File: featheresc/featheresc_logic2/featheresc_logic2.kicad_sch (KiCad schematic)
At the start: 24 parts, among them J1 RC IN 1, J2 RC IN 2, J3 soicbite prog connector, J7 Interconnect 1, J8 Interconnect 2, U1 AMS1117-50, U2 XL1509-ADJE1, U3 ATtiny1614-SS

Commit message: Update layout to be more compact, swap a few parts
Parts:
- J1, J2: footprint Connector_JST:JST_XA_S03B-XASK-1_1x03_P2.50mm_Horizontal -> Connector_JST:JST_XH_S3B-XH-A_1x03_P2.50mm_Horizontal
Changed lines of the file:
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@@
       (effects (font (size 1.27 1.27)) (justify right))
     )
-    (property "Footprint" "Connector_JST:JST_XA_S03B-XASK-1_1x03_P2.50mm_Horizontal" (id 2) (at 193.04 153.035 0)
+    (property "Footprint" "Connector_JST:JST_XH_S3B-XH-A_1x03_P2.50mm_Horizontal" (id 2) (at 193.04 153.035 0)
       (effects (font (size 1.27 1.27)) hide)
     )
@@
       (effects (font (size 1.27 1.27)) (justify right))
     )
-    (property "Footprint" "Connector_JST:JST_XA_S03B-XASK-1_1x03_P2.50mm_Horizontal" (id 2) (at 245.11 153.035 0)
+    (property "Footprint" "Connector_JST:JST_XH_S3B-XH-A_1x03_P2.50mm_Horizontal" (id 2) (at 245.11 153.035 0)
       (effects (font (size 1.27 1.27)) hide)
     )
@@
       (reference "#PWR04") (unit 1) (value "GND") (footprint "")
     )
-    (path "/d7d4c434-72cc-459d-9ec2-c8f3576f629f/52343ac2-4969-42df-af1e-ed7deb794aea"
-      (reference "#PWR05") (unit 1) (value "GND") (footprint "")
-    )
     (path "/96d38acb-e23b-424c-afed-fdd96c395092"
       (reference "#PWR06") (unit 1) (value "GND") (footprint "")
@@
       (reference "#PWR018") (unit 1) (value "GND") (footprint "")
     )
-    (path "/e21eb0e0-0c12-4a19-b0a2-2a3e790fd264/52343ac2-4969-42df-af1e-ed7deb794aea"
-      (reference "#PWR019") (unit 1) (value "GND") (footprint "")
-    )
     (path "/acde64c0-adac-4ba4-8f88-518b3a754432"
       (reference "#PWR020") (unit 1) (value "GND") (footprint "")
@@
       (reference "D8") (unit 1) (value "Red") (footprint "LED_SMD:LED_0805_2012Metric_Pad1.15x1.40mm_HandSolder")
     )
+    (path "/d7d4c434-72cc-459d-9ec2-c8f3576f629f/11cdec55-435f-4b7f-805a-bee9ab2b00ee"
+      (reference "D9") (unit 1) (value "Green") (footprint "LED_SMD:LED_0805_2012Metric_Pad1.15x1.40mm_HandSolder")
+    )
+    (path "/e21eb0e0-0c12-4a19-b0a2-2a3e790fd264/11cdec55-435f-4b7f-805a-bee9ab2b00ee"
+      (reference "D10") (unit 1) (value "Green") (footprint "LED_SMD:LED_0805_2012Metric_Pad1.15x1.40mm_HandSolder")
+    )
     (path "/232bbb65-7869-4831-a033-eb4672019cff"
       (reference "H1") (unit 1) (value "Interconnect M3") (footprint "MountingHole:MountingHole_3.2mm_M3")
@@
     )
     (path "/006e2d2d-ea55-4517-8464-6fa4323dbbb5"
-      (reference "J1") (unit 1) (value "RC IN 1") (footprint "Connector_JST:JST_XA_S03B-XASK-1_1x03_P2.50mm_Horizontal")
+      (reference "J1") (unit 1) (value "RC IN 1") (footprint "Connector_JST:JST_XH_S3B-XH-A_1x03_P2.50mm_Horizontal")
     )
     (path "/e6790c5d-2c5e-4728-8d92-8b5fc4b99492"
-      (reference "J2") (unit 1) (value "RC IN 2") (footprint "Connector_JST:JST_XA_S03B-XASK-1_1x03_P2.50mm_Horizontal")
+      (reference "J2") (unit 1) (value "RC IN 2") (footprint "Connector_JST:JST_XH_S3B-XH-A_1x03_P2.50mm_Horizontal")
     )
     (path "/8881e0dd-f100-4ed2-ac37-7908cdabe46b"

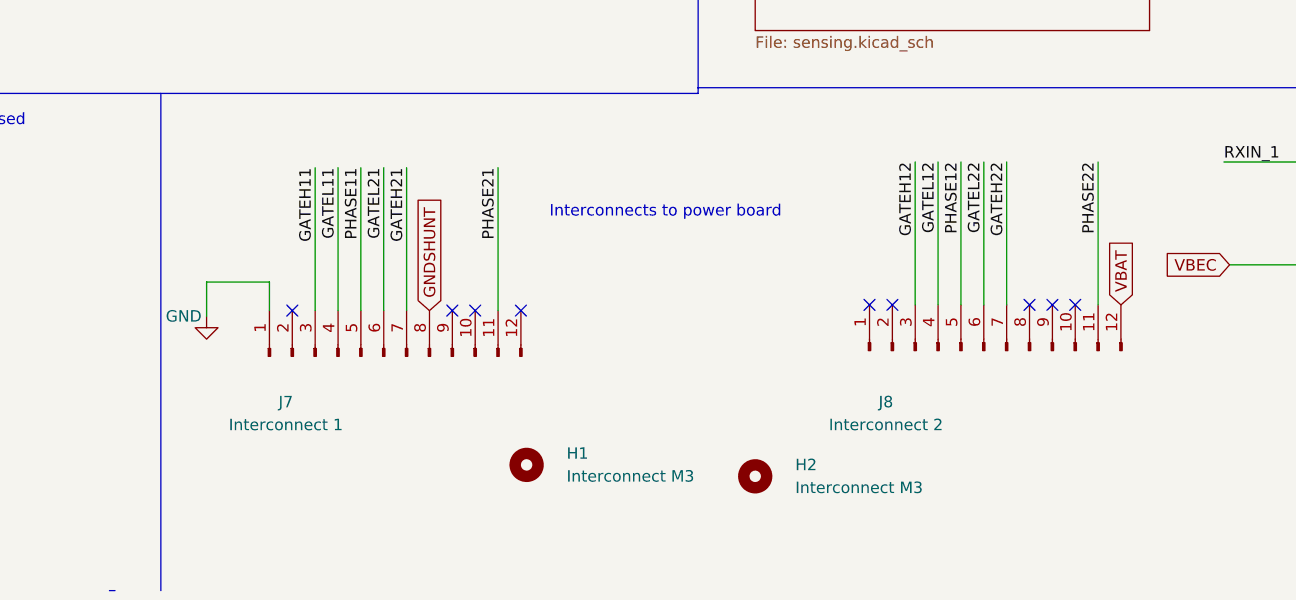
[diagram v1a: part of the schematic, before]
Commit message: improve interconnect pinouts
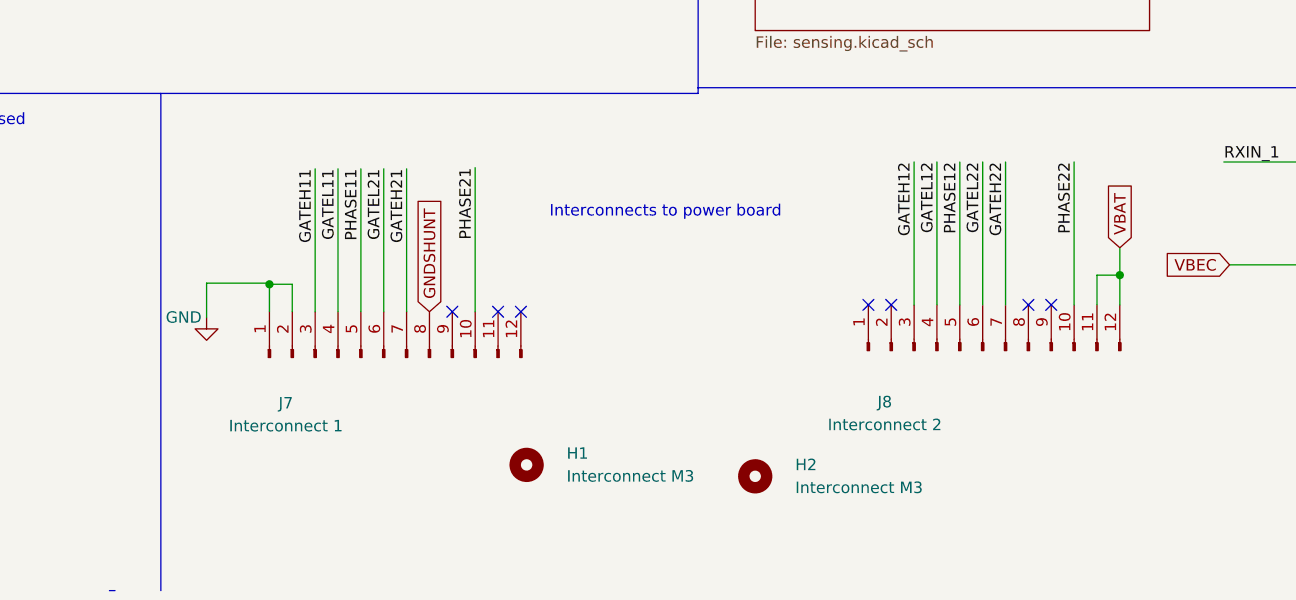
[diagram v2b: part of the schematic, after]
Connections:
- net GND: now also J7.2 (Pin_2)
- net PHASE21: now also J7.10 (Pin_10); no longer J7.11 (Pin_11)
- net PHASE22: now also J8.10 (Pin_10); no longer J8.11 (Pin_11)
- net VBAT: now also J8.11 (Pin_11)
- no-connect marks 14 -> 12

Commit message: Mixing switch
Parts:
- added R5: 33k, Resistor_SMD:R_0603_1608Metric_Pad0.98x0.95mm_HandSolder, symbol Device:R
- added SW1: SW_DIP_x01, Button_Switch_THT:SW_DIP_SPSTx01_Slide_6.7x4.1mm_W7.62mm_P2.54mm_LowProfile, symbol Switch:SW_DIP_x01
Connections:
- net GND: now also R5.2
- net TXDEBUG: now also SW1.1
- new net: R5.1, SW1.2
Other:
- note added: "Mixing on/off switch"
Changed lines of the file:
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@@
+    (stroke (width 0) (type default) (color 0 0 0 0))
+  )
+  (wire (pts (xy 79.248 113.538) (xy 79.248 118.618))
     (stroke (width 0) (type default) (color 0 0 0 0))
   )
@@
     (stroke (width 0) (type default) (color 0 0 0 0))
   )
+  (wire (pts (xy 53.848 113.538) (xy 36.703 113.538))
+    (stroke (width 0) (type default) (color 0 0 0 0))
+  )
   (wire (pts (xy 74.93 43.815) (xy 80.645 43.815))
     (stroke (width 0) (type default) (color 0 0 0 0))
@@
     (stroke (width 0) (type default) (color 0 0 0 0))
   )
+  (wire (pts (xy 76.708 113.538) (xy 79.248 113.538))
+    (stroke (width 0) (type default) (color 0 0 0 0))
+  )
   (wire (pts (xy 128.27 98.425) (xy 128.27 111.125))
     (stroke (width 0) (type default) (color 0 0 0 0))
@@
     (effects (font (size 1.27 1.27)) (justify left bottom))
   )
+  (text "Mixing on/off switch" (at 60.198 100.33 0)
+    (effects (font (size 1.27 1.27)) (justify left bottom))
+  )
   (text "Interconnects to power board" (at 93.345 156.845 0)
     (effects (font (size 1.27 1.27)) (justify left bottom))
@@
   )
   (label "MOTOREN_2" (at 127.635 59.055 0)
+    (effects (font (size 1.27 1.27)) (justify left bottom))
+  )
+  (label "TXDEBUG" (at 36.83 113.538 0)
     (effects (font (size 1.27 1.27)) (justify left bottom))
   )
@@
     (pin "1")
   )
+  (symbol (lib_id "Switch:SW_DIP_x01") (at 61.468 113.538 0) (unit 1)
+    (in_bom yes) (on_board yes) (fields_autoplaced)
+    (property "Reference" "SW1" (id 0) (at 61.468 105.156 0))
+    (property "Value" "SW_DIP_x01" (id 1) (at 61.468 107.696 0))
+    (property "Footprint" "Button_Switch_THT:SW_DIP_SPSTx01_Slide_6.7x4.1mm_W7.62mm_P2.54mm_LowProfile" (id 2) (at 61.468 113.538 0)
+      (effects (font (size 1.27 1.27)) hide)
+    )
+    (property "Datasheet" "~" (id 3) (at 61.468 113.538 0)
+      (effects (font (size 1.27 1.27)) hide)
+    )
+    (pin "1")
+    (pin "2")
+  )
   (symbol (lib_id "power:GND") (at 36.83 29.845 0) (unit 1)
     (in_bom yes) (on_board yes)
@@
     (pin "2")
   )
+  (symbol (lib_id "Device:R") (at 72.898 113.538 90) (unit 1)
+    (in_bom yes) (on_board yes)
+    (property "Reference" "R5" (id 0) (at 72.898 108.458 90))
+    (property "Value" "33k" (id 1) (at 72.898 110.998 90))
+    (property "Footprint" "Resistor_SMD:R_0603_1608Metric_Pad0.98x0.95mm_HandSolder" (id 2) (at 72.898 115.316 90)
+      (effects (font (size 1.27 1.27)) hide)
+    )
+    (property "Datasheet" "~" (id 3) (at 72.898 113.538 0)
+      (effects (font (size 1.27 1.27)) hide)
+    )
+    (pin "1")
+    (pin "2")
+  )
   (symbol (lib_id "Device:C") (at 27.305 55.245 0) (unit 1)
     (in_bom yes) (on_board yes)
@@
     (pin "1")
   )
+  (symbol (lib_id "power:GND") (at 79.248 118.618 0) (unit 1)
+    (in_bom yes) (on_board yes)
+    (property "Reference" "#PWR05" (id 0) (at 79.248 124.968 0)
+      (effects (font (size 1.27 1.27)) hide)
+    )
+    (property "Value" "GND" (id 1) (at 76.073 119.253 0))
+    (property "Footprint" "" (id 2) (at 79.248 118.618 0)
+      (effects (font (size 1.27 1.27)) hide)
+    )
+    (property "Datasheet" "" (id 3) (at 79.248 118.618 0)
+      (effects (font (size 1.27 1.27)) hide)
+    )
+    (pin "1")
+  )
   (symbol (lib_id "Connector:Conn_01x03_Male") (at 245.11 153.035 180) (unit 1)
     (in_bom yes) (on_board yes) (fields_autoplaced)
@@
       (reference "#PWR04") (unit 1) (value "GND") (footprint "")
     )
+    (path "/e195877b-b6ca-496d-ba2f-0f1c8774357e"
+      (reference "#PWR05") (unit 1) (value "GND") (footprint "")
+    )
     (path "/96d38acb-e23b-424c-afed-fdd96c395092"
       (reference "#PWR06") (unit 1) (value "GND") (footprint "")
@@
       (reference "R4") (unit 1) (value "1k") (footprint "Resistor_SMD:R_0603_1608Metric_Pad0.98x0.95mm_HandSolder")
     )
+    (path "/baafd01a-129d-4e9a-873d-a933cbcf4a0f"
+      (reference "R5") (unit 1) (value "33k") (footprint "Resistor_SMD:R_0603_1608Metric_Pad0.98x0.95mm_HandSolder")
+    )
     (path "/dad3c94d-671f-4606-a448-b81d24bd07d1"
       (reference "R7") (unit 1) (value "1k") (footprint "Resistor_SMD:R_0603_1608Metric_Pad0.98x0.95mm_HandSolder")
@@
       (reference "R15") (unit 1) (value "1k") (footprint "Resistor_SMD:R_0603_1608Metric_Pad0.98x0.95mm_HandSolder")
     )
+    (path "/35f8d9de-585d-42d2-90f9-1944b856b85e"
+      (reference "SW1") (unit 1) (value "SW_DIP_x01") (footprint "Button_Switch_THT:SW_DIP_SPSTx01_Slide_6.7x4.1mm_W7.62mm_P2.54mm_LowProfile")
+    )
     (path "/fcd53bb6-afcb-49c3-a34b-d9f070e5a3be"
